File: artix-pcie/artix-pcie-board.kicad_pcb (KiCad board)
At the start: 2 copper layers, 6 parts, among them P1 JTAG_CONN, U1 xc7a15tfgg484, U2 TOFE-4X, U3 N25Q256_QSPI, U4 AD9361, U5 xc7a15tcsg325

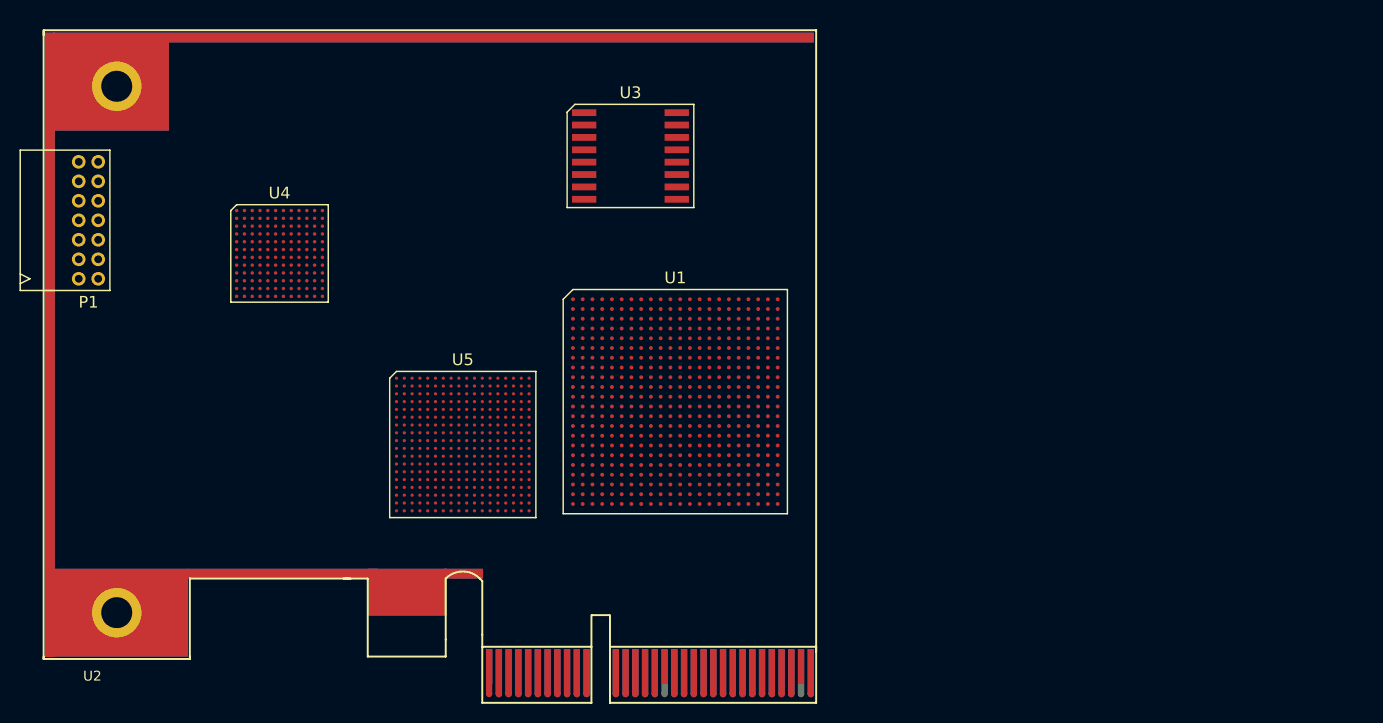
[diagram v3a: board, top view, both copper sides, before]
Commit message: wiring PCIe
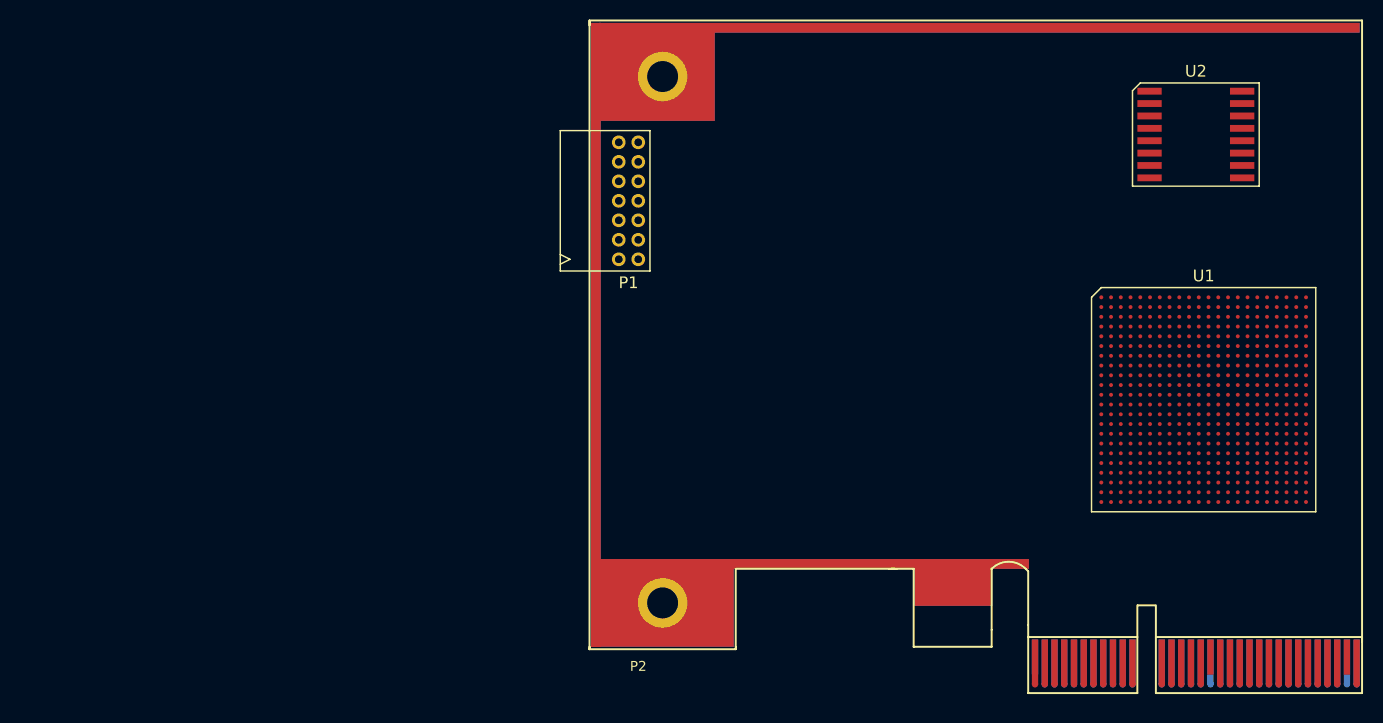
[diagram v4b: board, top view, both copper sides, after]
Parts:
- removed U3: N25Q256_QSPI, footlib:micron_SOP2-16
- removed U4: AD9361, footlib:AD9361
- removed U5: xc7a15tcsg325, footlib:Xil_Artix_CSG325
- added P2: TOFE-4X, footlib:TOFE_4X_HalfHeight, F.Cu at (108.0, 124.0)
- U2: value TOFE-4X -> N25Q256_QSPI; footprint TOFE_4X_HalfHeight -> footlib:micron_SOP2-16
- moved U2 129.9 mm to (170.2, 71.2), turned to 270 degrees
- moved P1 55.4 mm to (112.0, 78.0)
- moved U1 54.2 mm to (171.0, 98.4)
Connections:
- U1 pad A11: /GND -> Net-(U1-PadA11)
- U1 pad A12: /GND -> Net-(U1-PadA11)
- U1 pad A2: /GND -> Net-(U1-PadA11)
- U1 pad A22: /GND -> Net-(U1-PadA11)
- U1 pad A3: /GND -> Net-(U1-PadA11)
- U1 pad A5: /GND -> Net-(U1-PadA11)
- U1 pad A7: /GND -> Net-(U1-PadA11)
- U1 pad A9: /GND -> Net-(U1-PadA11)
- U1 pad AA12: /GND -> Net-(U1-PadA11)
- U1 pad AA17: /V2_5 -> Net-(U1-PadAA17)
- U1 pad AA2: /GND -> Net-(U1-PadA11)
- U1 pad AA22: /GND -> Net-(U1-PadA11)
- U1 pad AB14: /V2_5 -> Net-(U1-PadAA17)
- U1 pad AB19: /GND -> Net-(U1-PadA11)
- U1 pad AB9: /GND -> Net-(U1-PadA11)
- U1 pad B12: /GND -> Net-(U1-PadA11)
- U1 pad B19: /GND -> Net-(U1-PadA11)
- U1 pad B3: /GND -> Net-(U1-PadA11)
- U1 pad C1: /V2_5 -> Net-(U1-PadC1)
- U1 pad C10: /GND -> Net-(U1-PadA11)
- U1 pad C12: /GND -> Net-(U1-PadA11)
- U1 pad C16: /GND -> Net-(U1-PadA11)
- U1 pad C3: /GND -> Net-(U1-PadA11)
- U1 pad C6: /GND -> Net-(U1-PadA11)
- U1 pad D12: /GND -> Net-(U1-PadA11)
- U1 pad D13: /GND -> Net-(U1-PadA11)
- U1 pad D3: /GND -> Net-(U1-PadA11)
- U1 pad D4: /GND -> Net-(U1-PadA11)
- U1 pad D8: /GND -> Net-(U1-PadA11)
- U1 pad E11: /GND -> Net-(U1-PadA11)
- U1 pad E20: /GND -> Net-(U1-PadA11)
- U1 pad E4: /GND -> Net-(U1-PadA11)
- U1 pad E5: /GND -> Net-(U1-PadA11)
- U1 pad E7: /GND -> Net-(U1-PadA11)
- U1 pad E9: /GND -> Net-(U1-PadA11)
- U1 pad F11: /GND -> Net-(U1-PadA11)
- U1 pad F17: /GND -> Net-(U1-PadA11)
- U1 pad F2: /V2_5 -> Net-(U1-PadC1)
- U1 pad F5: /GND -> Net-(U1-PadA11)
- U1 pad G10: /GND -> Net-(U1-PadA11)
- U1 pad G12: /GND -> Net-(U1-PadA11)
- U1 pad G14: /GND -> Net-(U1-PadA11)
- U1 pad G5: /GND -> Net-(U1-PadA11)
- U1 pad G6: /GND -> Net-(U1-PadA11)
- U1 pad G7: /GND -> Net-(U1-PadA11)
- U1 pad G8: /GND -> Net-(U1-PadA11)
- U1 pad G9: /GND -> Net-(U1-PadA11)
- U1 pad H1: /GND -> Net-(U1-PadA11)
- U1 pad H11: /GND -> Net-(U1-PadA11)
- U1 pad H21: /GND -> Net-(U1-PadA11)
- U1 pad H6: /V2_5 -> Net-(U1-PadC1)
- U1 pad H7: /GND -> Net-(U1-PadA11)
- U1 pad H9: /GND -> Net-(U1-PadA11)
- U1 pad J10: /GND -> Net-(U1-PadA11)
- U1 pad J12: /GND -> Net-(U1-PadA11)
- U1 pad J18: /GND -> Net-(U1-PadA11)
- U1 pad J3: /V2_5 -> Net-(U1-PadC1)
- U1 pad J8: /GND -> Net-(U1-PadA11)
- U1 pad K11: /GND -> Net-(U1-PadA11)
- U1 pad K15: /GND -> Net-(U1-PadA11)
- U1 pad K5: /GND -> Net-(U1-PadA11)
- U1 pad K7: /GND -> Net-(U1-PadA11)
- U1 pad L2: /GND -> Net-(U1-PadA11)
- U1 pad L22: /GND -> Net-(U1-PadA11)
- U1 pad L8: /GND -> Net-(U1-PadA11)
- U1 pad M11: /GND -> Net-(U1-PadA11)
- U1 pad M19: /GND -> Net-(U1-PadA11)
- U1 pad M4: /V2_5 -> Net-(U1-PadC1)
- U1 pad M7: /GND -> Net-(U1-PadA11)
- U1 pad N1: /V2_5 -> Net-(U1-PadC1)
- U1 pad N16: /GND -> Net-(U1-PadA11)
- U1 pad N6: /GND -> Net-(U1-PadA11)
- U1 pad N8: /GND -> Net-(U1-PadA11)
- U1 pad P11: /GND -> Net-(U1-PadA11)
- U1 pad P13: /GND -> Net-(U1-PadA11)
- U1 pad P3: /GND -> Net-(U1-PadA11)
- U1 pad P7: /GND -> Net-(U1-PadA11)
- U1 pad P9: /GND -> Net-(U1-PadA11)
- U1 pad R10: /GND -> Net-(U1-PadA11)
- U1 pad R12: /GND -> Net-(U1-PadA11)
- U1 pad R20: /GND -> Net-(U1-PadA11)
- U1 pad R8: /GND -> Net-(U1-PadA11)
- U1 pad T11: /GND -> Net-(U1-PadA11)
- U1 pad T17: /GND -> Net-(U1-PadA11)
- U1 pad T7: /GND -> Net-(U1-PadA11)
- U1 pad T9: /GND -> Net-(U1-PadA11)
- U1 pad U14: /GND -> Net-(U1-PadA11)
- U1 pad U4: /GND -> Net-(U1-PadA11)
- U1 pad V1: /GND -> Net-(U1-PadA11)
- U1 pad V11: /GND -> Net-(U1-PadA11)
- U1 pad V16: /V2_5 -> Net-(U1-PadAA17)
- U1 pad V21: /GND -> Net-(U1-PadA11)
- U1 pad W13: /V2_5 -> Net-(U1-PadAA17)
- U1 pad W18: /GND -> Net-(U1-PadA11)
- U1 pad W8: /GND -> Net-(U1-PadA11)
- U1 pad Y10: /V2_5 -> Net-(U1-PadAA17)
- U1 pad Y15: /GND -> Net-(U1-PadA11)
- U1 pad Y5: /GND -> Net-(U1-PadA11)
